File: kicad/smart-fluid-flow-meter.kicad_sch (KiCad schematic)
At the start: 14 parts, among them J1 YF-S201, J2 Barrel_Jack, SW1 Factory reset button, U2 ESP32-DevkitV1

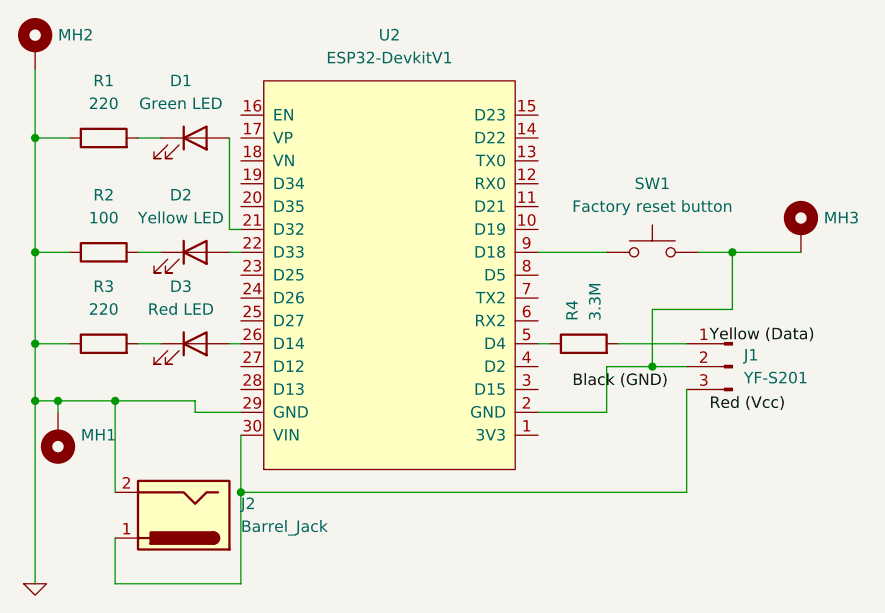
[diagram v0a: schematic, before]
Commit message: Fix Electrical Rules Checker errors. Fixes #73
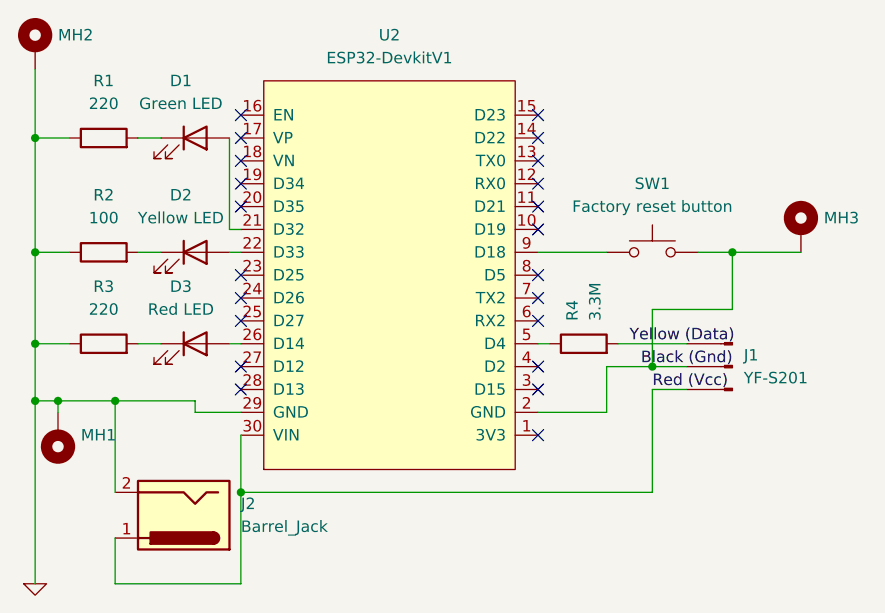
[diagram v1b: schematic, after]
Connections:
- net Red (Vcc): now also J1.3 (Pin_3), J2.1, U2.30 (VIN)
- net Yellow (Data): now also J1.1 (Pin_1), R4.2
- net Black (Gnd): now reaches J1.2 (Pin_2), MH3.1, SW1.2, U2.2 (GND)
- no-connect marks 0 -> 22
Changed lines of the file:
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@@
 		(color 0 0 0 0)
 	)
+	(no_connect
+		(at 128.27 55.88)
+	)
+	(no_connect
+		(at 128.27 81.28)
+	)
+	(no_connect
+		(at 95.25 68.58)
+	)
+	(no_connect
+		(at 128.27 68.58)
+	)
+	(no_connect
+		(at 95.25 63.5)
+	)
+	(no_connect
+		(at 95.25 66.04)
+	)
+	(no_connect
+		(at 128.27 48.26)
+	)
+	(no_connect
+		(at 95.25 76.2)
+	)
+	(no_connect
+		(at 95.25 53.34)
+	)
+	(no_connect
+		(at 95.25 55.88)
+	)
+	(no_connect
+		(at 95.25 73.66)
+	)
+	(no_connect
+		(at 128.27 76.2)
+	)
+	(no_connect
+		(at 128.27 73.66)
+	)
+	(no_connect
+		(at 128.27 53.34)
+	)
+	(no_connect
+		(at 95.25 45.72)
+	)
+	(no_connect
+		(at 95.25 50.8)
+	)
+	(no_connect
+		(at 95.25 48.26)
+	)
+	(no_connect
+		(at 128.27 63.5)
+	)
+	(no_connect
+		(at 128.27 50.8)
+	)
+	(no_connect
+		(at 128.27 45.72)
+	)
+	(no_connect
+		(at 128.27 66.04)
+	)
+	(no_connect
+		(at 128.27 58.42)
+	)
 	(wire
 		(pts
@@
 	(wire
 		(pts
+			(xy 72.39 48.26) (xy 76.2 48.26)
+		)
+		(stroke
+			(width 0)
+			(type default)
+		)
+	)
+	(wire
+		(pts
+			(xy 76.2 60.96) (xy 72.39 60.96)
+		)
+		(stroke
+			(width 0)
+			(type default)
+		)
+	)
+	(wire
+		(pts
+			(xy 137.16 71.12) (xy 144.78 71.12)
+		)
+		(stroke
+			(width 0)
+			(type default)
+		)
+	)
+	(wire
+		(pts
+			(xy 72.39 40.64) (xy 72.39 48.26)
+		)
+		(stroke
+			(width 0)
+			(type default)
+		)
+	)
+	(wire
+		(pts
+			(xy 140.97 76.2) (xy 144.78 76.2)
+		)
+		(stroke
+			(width 0)
+			(type default)
+		)
+	)
+	(wire
+		(pts
+			(xy 83.82 71.12) (xy 86.36 71.12)
+		)
+		(stroke
+			(width 0)
+			(type default)
+		)
+	)
+	(wire
+		(pts
+			(xy 146.05 60.96) (xy 149.86 60.96)
+		)
+		(stroke
+			(width 0)
+			(type default)
+		)
+	)
+	(wire
+		(pts
+			(xy 72.39 77.47) (xy 74.93 77.47)
+		)
+		(stroke
+			(width 0)
+			(type default)
+		)
+	)
+	(wire
+		(pts
+			(xy 95.25 78.74) (xy 90.17 78.74)
+		)
+		(stroke
+			(width 0)
+			(type default)
+		)
+	)
+	(wire
+		(pts
+			(xy 149.86 60.96) (xy 149.86 67.31)
+		)
+		(stroke
+			(width 0)
+			(type default)
+		)
+	)
+	(wire
+		(pts
+			(xy 72.39 71.12) (xy 72.39 77.47)
+		)
+		(stroke
+			(width 0)
+			(type default)
+		)
+	)
+	(wire
+		(pts
+			(xy 95.25 58.42) (xy 93.98 58.42)
+		)
+		(stroke
+			(width 0)
+			(type default)
+		)
+	)
+	(wire
+		(pts
+			(xy 93.98 58.42) (xy 93.98 48.26)
+		)
+		(stroke
+			(width 0)
+			(type default)
+		)
+	)
+	(wire
+		(pts
+			(xy 72.39 60.96) (xy 72.39 71.12)
+		)
+		(stroke
+			(width 0)
+			(type default)
+		)
+	)
+	(wire
+		(pts
+			(xy 149.86 60.96) (xy 157.48 60.96)
+		)
+		(stroke
+			(width 0)
+			(type default)
+		)
+	)
+	(wire
+		(pts
+			(xy 74.93 77.47) (xy 74.93 78.74)
+		)
+		(stroke
+			(width 0)
+			(type default)
+		)
+	)
+	(wire
+		(pts
+			(xy 140.97 67.31) (xy 140.97 73.66)
+		)
+		(stroke
+			(width 0)
+			(type default)
+		)
+	)
+	(wire
+		(pts
+			(xy 72.39 71.12) (xy 76.2 71.12)
+		)
+		(stroke
+			(width 0)
+			(type default)
+		)
+	)
+	(wire
+		(pts
+			(xy 86.36 60.96) (xy 83.82 60.96)
+		)
+		(stroke
+			(width 0)
+			(type default)
+		)
+	)
+	(wire
+		(pts
 			(xy 140.97 73.66) (xy 144.78 73.66)
 		)
@@
 	(wire
 		(pts
-			(xy 72.39 48.26) (xy 76.2 48.26)
-		)
-		(stroke
-			(width 0)
-			(type default)
-		)
-	)
-	(wire
-		(pts
-			(xy 76.2 60.96) (xy 72.39 60.96)
-		)
-		(stroke
-			(width 0)
-			(type default)
-		)
-	)
-	(wire
-		(pts
-			(xy 137.16 71.12) (xy 144.78 71.12)
-		)
-		(stroke
-			(width 0)
-			(type default)
-		)
-	)
-	(wire
-		(pts
-			(xy 72.39 40.64) (xy 72.39 48.26)
-		)
-		(stroke
-			(width 0)
-			(type default)
-		)
-	)
-	(wire
-		(pts
-			(xy 83.82 71.12) (xy 86.36 71.12)
-		)
-		(stroke
-			(width 0)
-			(type default)
-		)
-	)
-	(wire
-		(pts
-			(xy 146.05 60.96) (xy 149.86 60.96)
-		)
-		(stroke
-			(width 0)
-			(type default)
-		)
-	)
-	(wire
-		(pts
-			(xy 72.39 77.47) (xy 74.93 77.47)
-		)
-		(stroke
-			(width 0)
-			(type default)
-		)
-	)
-	(wire
-		(pts
-			(xy 95.25 78.74) (xy 90.17 78.74)
-		)
-		(stroke
-			(width 0)
-			(type default)
-		)
-	)
-	(wire
-		(pts
-			(xy 149.86 60.96) (xy 149.86 67.31)
-		)
-		(stroke
-			(width 0)
-			(type default)
-		)
-	)
-	(wire
-		(pts
-			(xy 72.39 71.12) (xy 72.39 77.47)
-		)
-		(stroke
-			(width 0)
-			(type default)
-		)
-	)
-	(wire
-		(pts
-			(xy 95.25 58.42) (xy 93.98 58.42)
-		)
-		(stroke
-			(width 0)
-			(type default)
-		)
-	)
-	(wire
-		(pts
-			(xy 93.98 58.42) (xy 93.98 48.26)
-		)
-		(stroke
-			(width 0)
-			(type default)
-		)
-	)
-	(wire
-		(pts
-			(xy 72.39 60.96) (xy 72.39 71.12)
-		)
-		(stroke
-			(width 0)
-			(type default)
-		)
-	)
-	(wire
-		(pts
-			(xy 149.86 60.96) (xy 157.48 60.96)
-		)
-		(stroke
-			(width 0)
-			(type default)
-		)
-	)
-	(wire
-		(pts
-			(xy 74.93 77.47) (xy 74.93 78.74)
-		)
-		(stroke
-			(width 0)
-			(type default)
-		)
-	)
-	(wire
-		(pts
-			(xy 140.97 67.31) (xy 140.97 73.66)
-		)
-		(stroke
-			(width 0)
-			(type default)
-		)
-	)
-	(wire
-		(pts
-			(xy 72.39 71.12) (xy 76.2 71.12)
-		)
-		(stroke
-			(width 0)
-			(type default)
-		)
-	)
-	(wire
-		(pts
-			(xy 86.36 60.96) (xy 83.82 60.96)
-		)
-		(stroke
-			(width 0)
-			(type default)
-		)
-	)
-	(wire
-		(pts
 			(xy 74.93 77.47) (xy 81.28 77.47)
 		)
@@
 	(wire
 		(pts
-			(xy 144.78 76.2) (xy 144.78 87.63)
-		)
-		(stroke
-			(width 0)
-			(type default)
-		)
-	)
-	(wire
-		(pts
-			(xy 95.25 87.63) (xy 144.78 87.63)
+			(xy 140.97 76.2) (xy 140.97 87.63)
+		)
+		(stroke
+			(width 0)
+			(type default)
+		)
+	)
+	(wire
+		(pts
+			(xy 95.25 87.63) (xy 140.97 87.63)
 		)
 		(stroke
@@
 		)
 	)
-	(label "Black (GND)"
-		(at 132.08 76.2 0)
+	(label "Black (Gnd)"
+		(at 139.7 73.66 0)
 		(fields_autoplaced yes)
 		(effects
@@
 	)
 	(label "Yellow (Data)"
-		(at 147.32 71.12 0)
+		(at 138.43 71.12 0)
 		(fields_autoplaced yes)
 		(effects
@@
 	)
 	(label "Red (Vcc)"
-		(at 147.32 78.74 0)
+		(at 140.97 76.2 0)
 		(fields_autoplaced yes)
 		(effects
